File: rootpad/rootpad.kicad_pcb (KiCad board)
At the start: 2 copper layers, 77.8 x 110.3 mm, 56 parts, among them J1 USB_B_Mini, SW1 SW_Push, U1 ATmega32U4-AU, Y1 16MHz

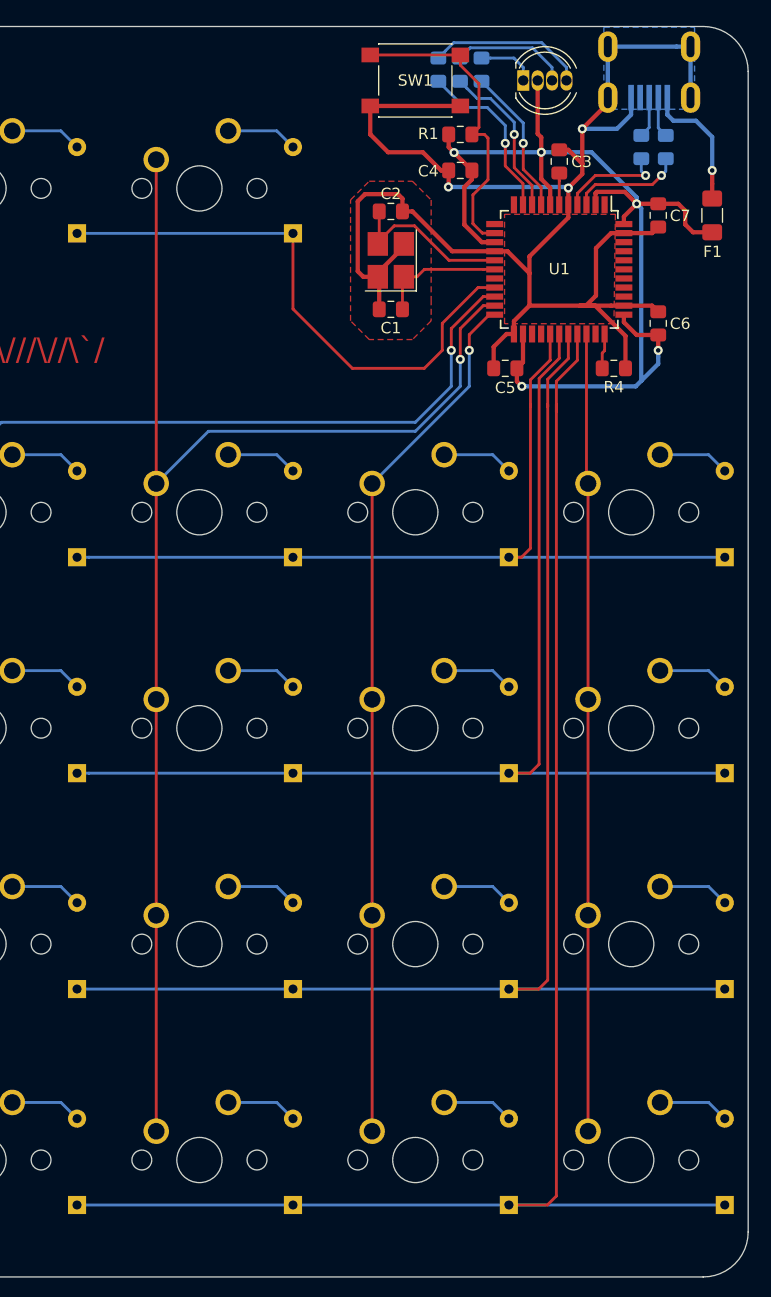
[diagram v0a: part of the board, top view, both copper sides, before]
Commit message: Moved libraries and implemented changes from ai03 branch
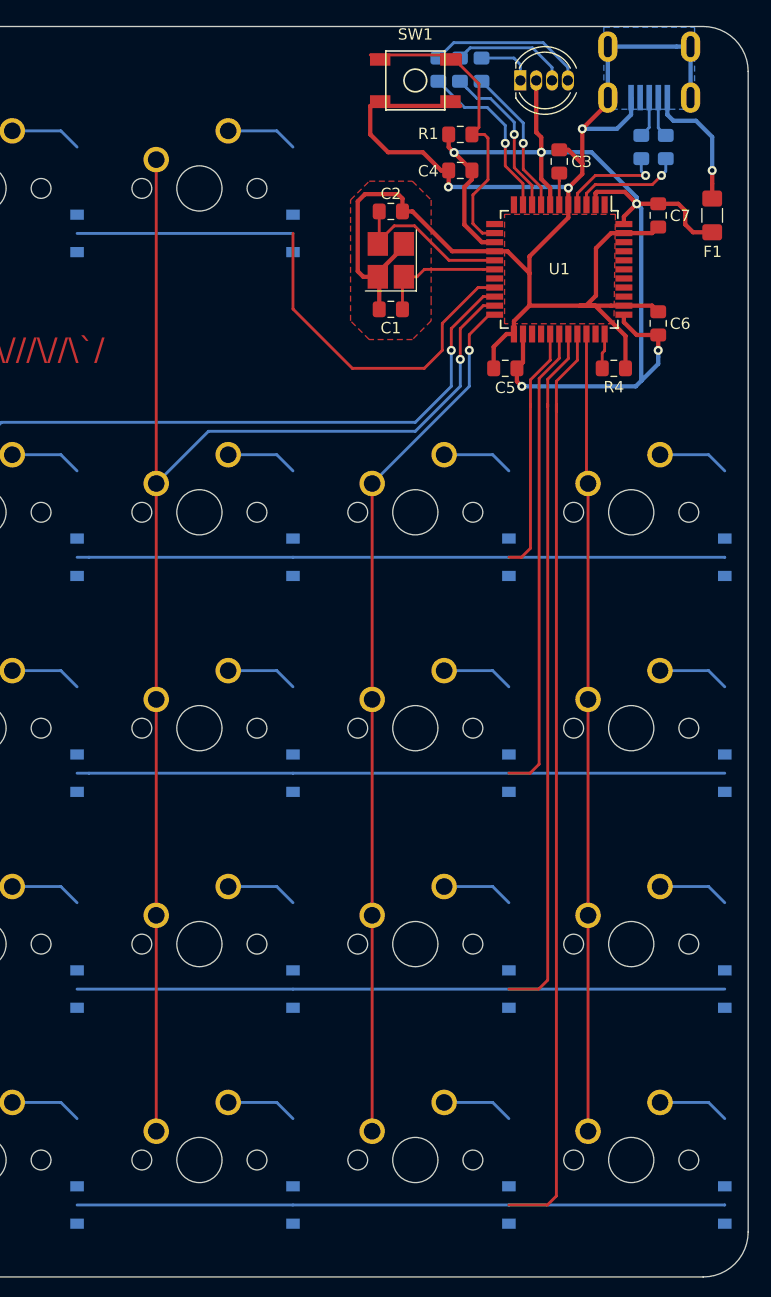
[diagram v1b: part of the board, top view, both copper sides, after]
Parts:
- D1, D10, D11, D12, D13, D14, D15, D16, D17, D18, D2, D3, D4, D5, D6, D7, D8, D9: footprint Diode_THT:D_DO-35_SOD27_P7.62mm_Horizontal -> Diode_SMD:D_SOD-123
- D19: footprint LED_THT:LED_D5.0mm-4_RGB -> random-keyboard-parts:LED_D5.0mm-4_RGB_Spaced
- SW1: footprint Button_Switch_SMD:SW_Push_1P1T_NO_6x6mm_H9.5mm -> random-keyboard-parts:SKQG-1155865

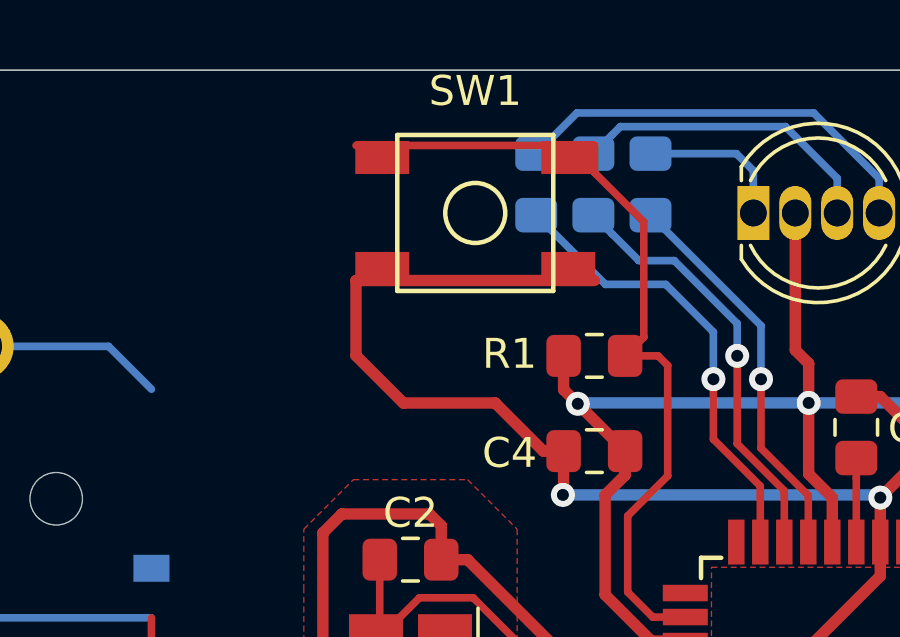
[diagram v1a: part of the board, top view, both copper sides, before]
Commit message: Correctly routed reset button
Diodes still need work done
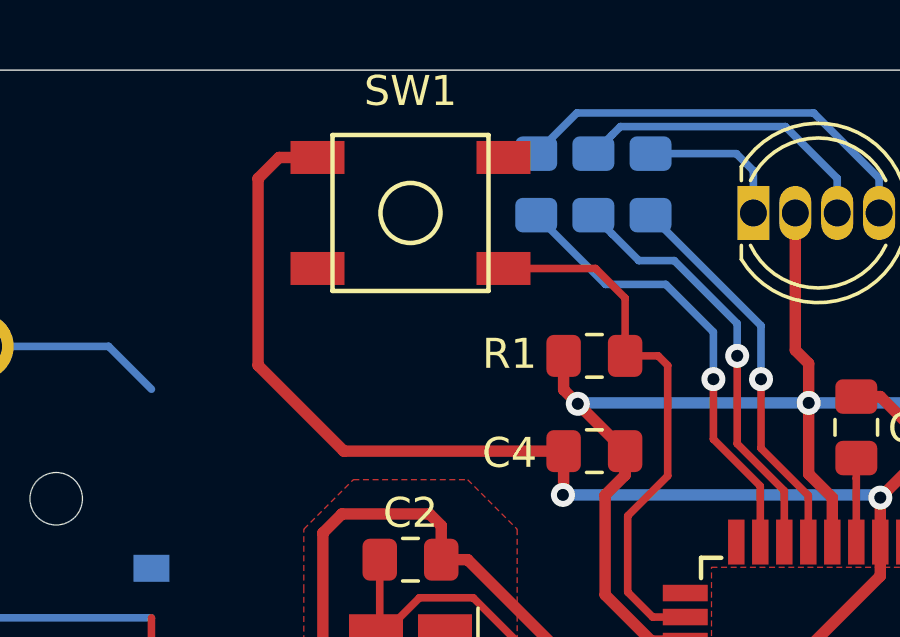
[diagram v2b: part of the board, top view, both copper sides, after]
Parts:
- moved SW1 2.16 mm to (166.1, 50.8)
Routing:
- net Net-(R1-Pad2): track 27.8 -> 18.3 mm
- net GND: track 149.5 -> 150.7 mm
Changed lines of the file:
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@@
     (thickness 1.6)
     (drawings 10)
-    (tracks 339)
+    (tracks 336)
     (zones 0)
     (modules 56)
@@
   )
   (module random-keyboard-parts:SKQG-1155865 (layer F.Cu)
-    (at 168.275 50.8 180)
+    (at 166.116 50.8 180)
     (attr smd)
     (fp_text reference SW1 (at 0 4.064) (layer F.SilkS)
@@
   (segment (start 187.3125 53.8215) (end 186.06427 55.06973) (width 0.381) (layer B.Cu) (net 1))
   (segment (start 187.3125 52.3155) (end 187.3125 53.8215) (width 0.381) (layer B.Cu) (net 1))
-  (segment (start 164.3 55.55625) (end 164.3 53.05) (width 0.381) (layer F.Cu) (net 1))
-  (segment (start 164.3 53.05) (end 172.25 53.05) (width 0.381) (layer F.Cu) (net 1))
-  (segment (start 168.940375 57.134125) (end 165.877875 57.134125) (width 0.381) (layer F.Cu) (net 1))
-  (segment (start 170.54502 58.73877) (end 168.940375 57.134125) (width 0.381) (layer F.Cu) (net 1))
-  (segment (start 171.22002 58.73877) (end 170.54502 58.73877) (width 0.381) (layer F.Cu) (net 1))
-  (segment (start 165.877875 57.134125) (end 164.3 55.55625) (width 0.381) (layer F.Cu) (net 1))
   (via (at 171.196 60.198) (size 0.8) (drill 0.4) (layers F.Cu B.Cu) (net 1))
   (segment (start 171.22002 58.73877) (end 171.22002 60.17398) (width 0.381) (layer F.Cu) (net 1))
@@
   (segment (start 167.266 65.472098) (end 164.966 67.772098) (width 0.381) (layer F.Cu) (net 1))
   (segment (start 167.266 65.225) (end 167.266 65.472098) (width 0.381) (layer F.Cu) (net 1))
+  (segment (start 161.036 55.88) (end 163.89477 58.73877) (width 0.381) (layer F.Cu) (net 1))
+  (segment (start 161.036 49.649) (end 161.036 55.88) (width 0.381) (layer F.Cu) (net 1))
+  (segment (start 163.016 48.95) (end 161.735 48.95) (width 0.381) (layer F.Cu) (net 1))
+  (segment (start 163.89477 58.73877) (end 171.22002 58.73877) (width 0.381) (layer F.Cu) (net 1))
+  (segment (start 161.735 48.95) (end 161.036 49.649) (width 0.381) (layer F.Cu) (net 1))
   (segment (start 167.141 68.25) (end 167.266 68.125) (width 0.254) (layer F.Cu) (net 2))
   (segment (start 167.141 70.993) (end 167.141 68.25) (width 0.254) (layer F.Cu) (net 2))
@@
   (segment (start 174.68977 55.88127) (end 174.68977 59.56427) (width 0.254) (layer F.Cu) (net 35))
   (segment (start 174.37227 55.56377) (end 174.68977 55.88127) (width 0.254) (layer F.Cu) (net 35))
-  (segment (start 172.25 49.454) (end 172.25 48.55) (width 0.254) (layer F.Cu) (net 35))
-  (segment (start 173.893392 51.097392) (end 172.25 49.454) (width 0.254) (layer F.Cu) (net 35))
-  (segment (start 173.893392 54.940398) (end 173.893392 51.097392) (width 0.254) (layer F.Cu) (net 35))
-  (segment (start 173.27002 55.56377) (end 173.893392 54.940398) (width 0.254) (layer F.Cu) (net 35))
-  (segment (start 164.3 48.55) (end 172.25 48.55) (width 0.254) (layer F.Cu) (net 35))
+  (segment (start 173.27002 55.56377) (end 173.27002 53.63602) (width 0.254) (layer F.Cu) (net 35))
+  (segment (start 172.284 52.65) (end 169.216 52.65) (width 0.254) (layer F.Cu) (net 35))
+  (segment (start 173.27002 53.63602) (end 172.284 52.65) (width 0.254) (layer F.Cu) (net 35))
   (segment (start 188.9125 54.95279) (end 188.21527 55.65002) (width 0.254) (layer B.Cu) (net 36))
   (segment (start 188.9125 52.3155) (end 188.9125 54.95279) (width 0.254) (layer B.Cu) (net 36))

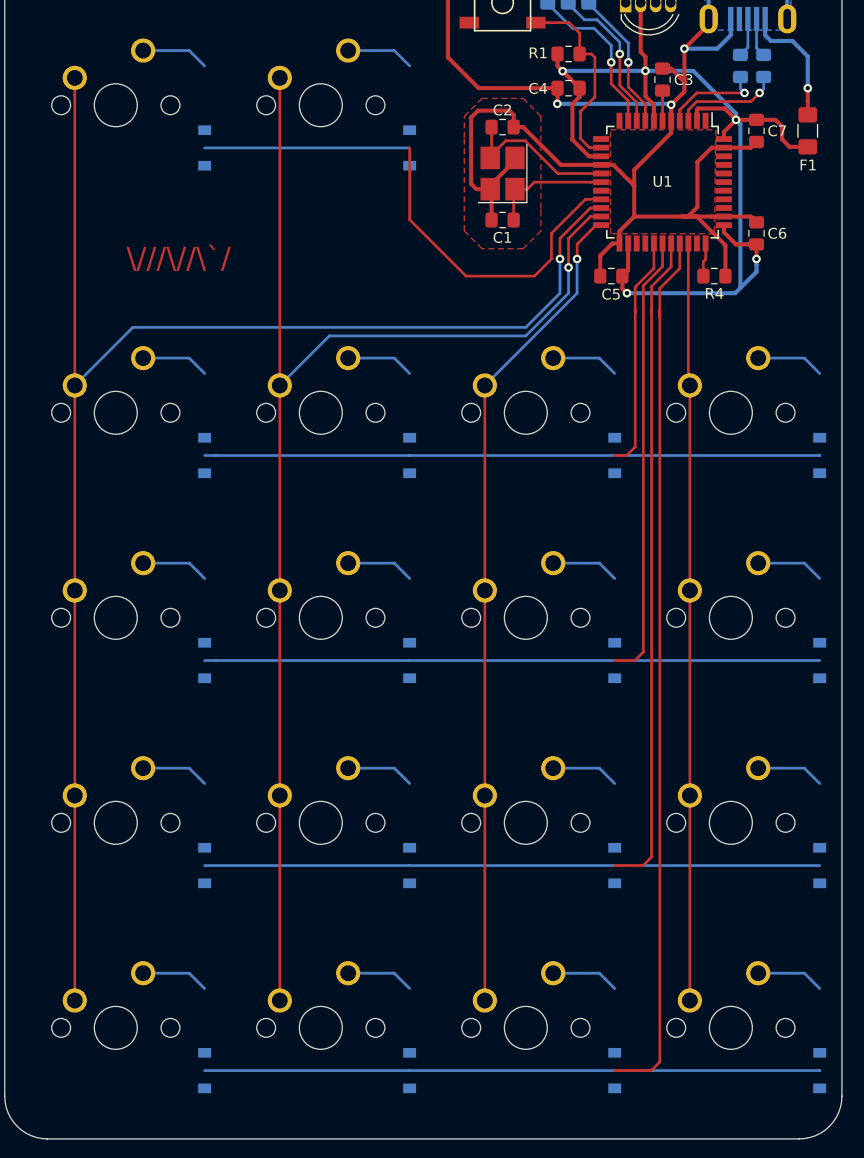
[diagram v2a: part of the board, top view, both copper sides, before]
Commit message: Routed Diodes, need to move name
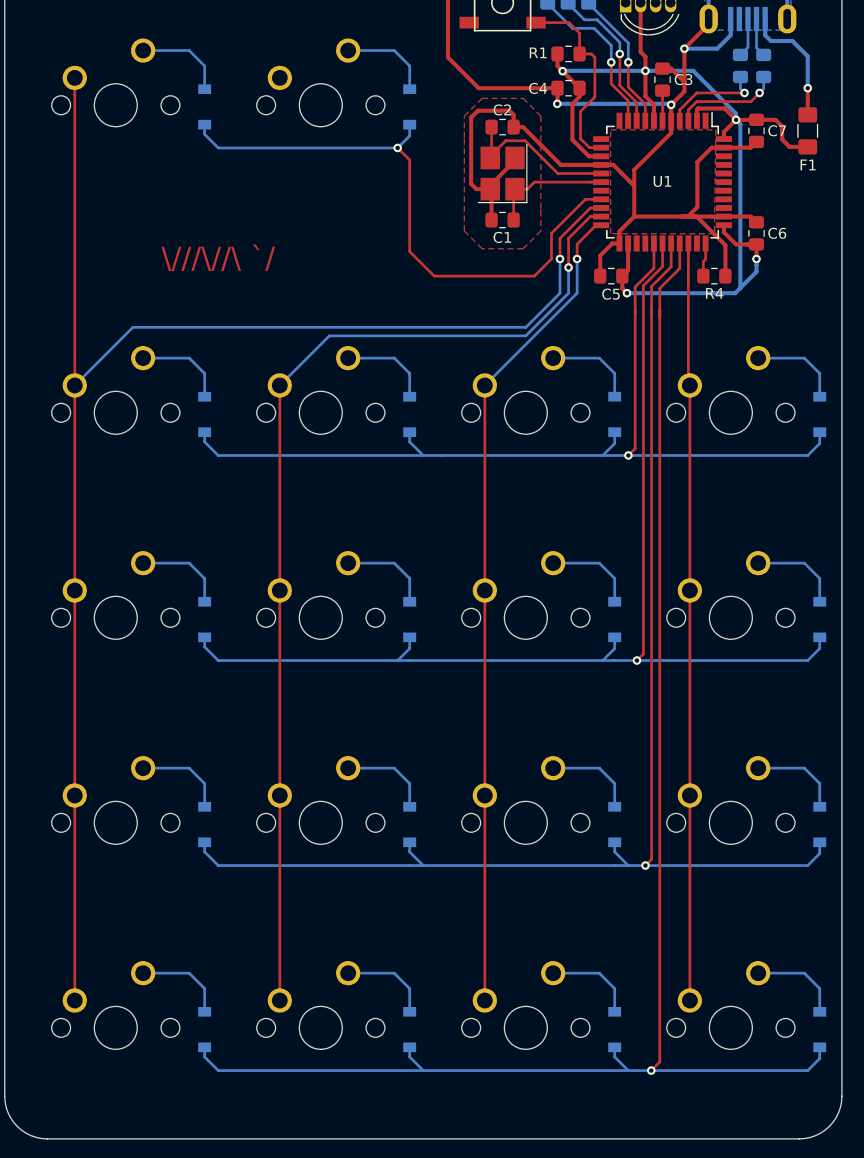
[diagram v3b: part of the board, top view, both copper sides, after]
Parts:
- moved D11 3.81 mm to (138.4, 127.2)
- moved D12 3.81 mm to (157.5, 127.2)
- moved D13 3.81 mm to (176.5, 127.2)
- moved D14 3.81 mm to (195.6, 127.2)
- moved D15 3.81 mm to (138.4, 146.2)
- moved D16 3.81 mm to (157.5, 146.2)
- moved D17 3.81 mm to (176.5, 146.2)
- moved D18 3.81 mm to (195.6, 146.2)
- moved D3 3.81 mm to (138.4, 89.1)
- moved D4 3.81 mm to (157.5, 89.1)
- moved D5 3.81 mm to (176.5, 89.1)
- moved D6 3.81 mm to (195.6, 89.1)
- moved D1 3.81 mm to (138.4, 60.5)
- moved D2 3.81 mm to (157.5, 60.5)
- moved D10 3.81 mm to (195.6, 108.1)
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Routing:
- net COL1: track 125.1 -> 96.5 mm
- net ROW1: track 79.2 -> 86.3 mm, vias 0 -> 1
- net ROW2: track 98.8 -> 105.1 mm, vias 0 -> 1
- net ROW3: track 118.9 -> 124.4 mm, vias 0 -> 1
- net ROW0: track 50.0 -> 55.1 mm, vias 0 -> 1
- net ROW4: track 139.1 -> 144.0 mm, vias 0 -> 1
- net Net-(D9-Pad2): track 6.31 -> 8.47 mm
- net Net-(D8-Pad2): track 6.31 -> 8.47 mm
- net Net-(D7-Pad2): track 6.31 -> 8.47 mm
- net Net-(D6-Pad2): track 6.31 -> 8.47 mm
- net Net-(D4-Pad2): track 6.31 -> 8.47 mm
- net Net-(D3-Pad2): track 6.31 -> 8.47 mm
- net Net-(D2-Pad2): track 6.31 -> 8.47 mm
- net Net-(D18-Pad2): track 6.31 -> 8.47 mm
- net Net-(D16-Pad2): track 6.31 -> 8.47 mm
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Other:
- board text added: "\///\//\ `/"
- board text removed: "\///\//\`/"
